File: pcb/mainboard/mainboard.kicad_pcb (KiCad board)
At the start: 10 copper layers, 165 x 121 mm, 629 parts, among them J1 CONN_PCIE_PWR_8PIN, J10 FAN_01, J11 XILINX_JTAG, J12 JUMPER_0402_SPDT, J13 JUMPER_0402_SPDT, J14 RJ45, J15 PMOD_HOST, J16 SMPM, J17 SMPM, J18 SMPM, J19 SMPM, J2 CONN_IBC_MGMT, J20 SMPM, J21 SMPM, J22 SMPM, J23 SMPM, J24 SMPM, J25 SMPM, J26 SMPM, J27 0826-1G1T-23-F, J28 SMPM, J29 SMPM, J3 CONN_01X03, J30 SMPM, J31 SMPM, J32 SMPM, J33 SMPM, J34 SMPM, J35 SMPM, J36 SMPM, J37 SMPM, J38 SMPM, J39 SMPM, J4 CONN_01X05, J40 SMPM, J41 SMPM, J42 SMPM, J43 SMPM, J44 SMPM, J45 SMPM, J46 SMPM, J47 SMPM, J48 CONN_01X10, J5 XILINX_JTAG, J6 CONN_SFP_HOST, J7 SFP_CAGE, J8 FAN_01, J9 CONN_01X03, K1 RELAY_TE_HF3_96, K2 RELAY_TE_HF3_96, K3 RELAY_TE_HF3_96, K4 RELAY_TE_HF3_96, M1 960-23-23-F-AB-0, SW1 SWITCH, SW2 SWITCH, U1 STM32L031C6U6, U10 MAX40026, U11 MAX40026, U12 MAX40026, U13 MAX40026, U14 MAX40026, U15 MAX40026, U16 MAX40026, U17 MAX40026, U18 MAX40026, U19 MAX40026, U2 MYMGK1R812ERSR, U20 MAX40026, U21 DAC60508, U22 DAC60508, U23 STM32H735-UFBGA176-25, U24 AT24MAC402, U25 ADM3101E_QFN, U26 LMR70503, U27 SIT9121AI-2BF-XXS200.000000G, U28 SIT9121AI-2BF-XXS156.250000G, U29 HMC675LP3E, U3 MYMGK00504ERSR, U30 SIT9121AI-2BF-XXS200.000000G, U31 ECS-1612MV-250-CN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

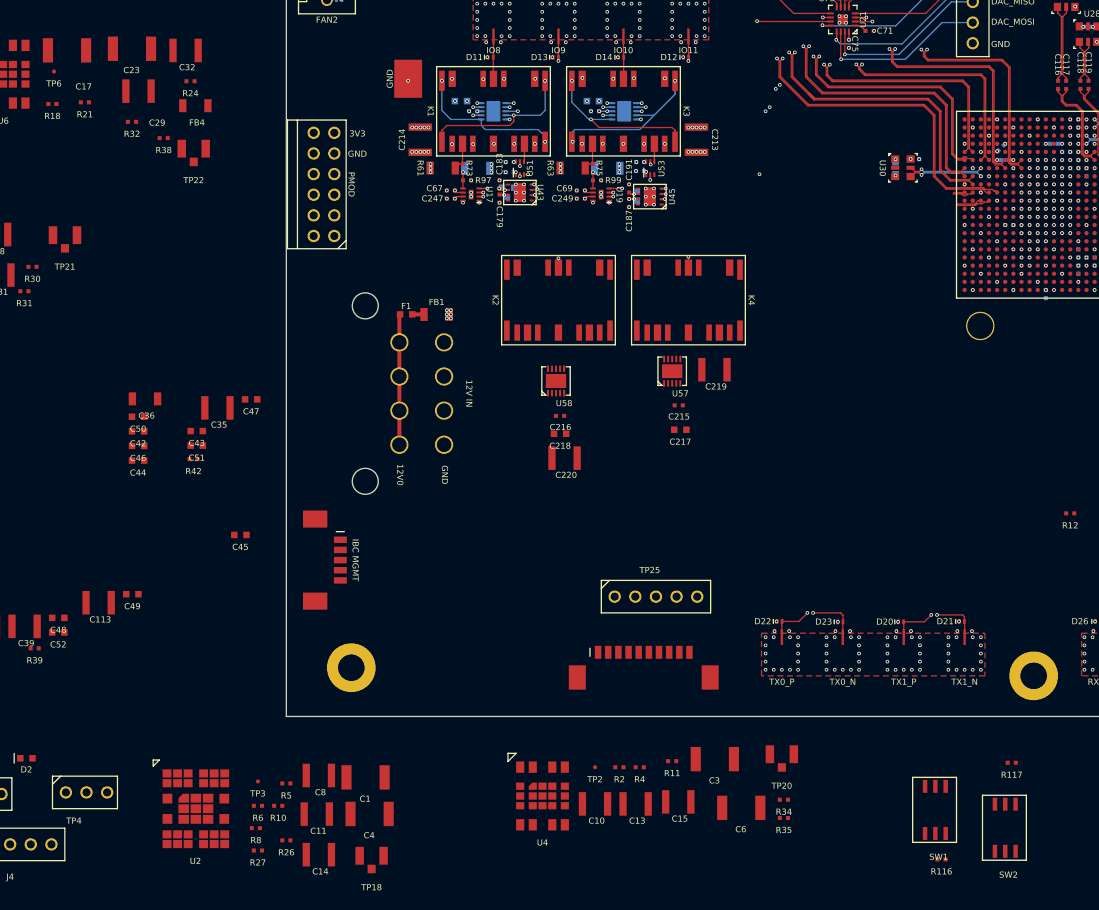
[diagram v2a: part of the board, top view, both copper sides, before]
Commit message: Placed remainder of relays and drivers
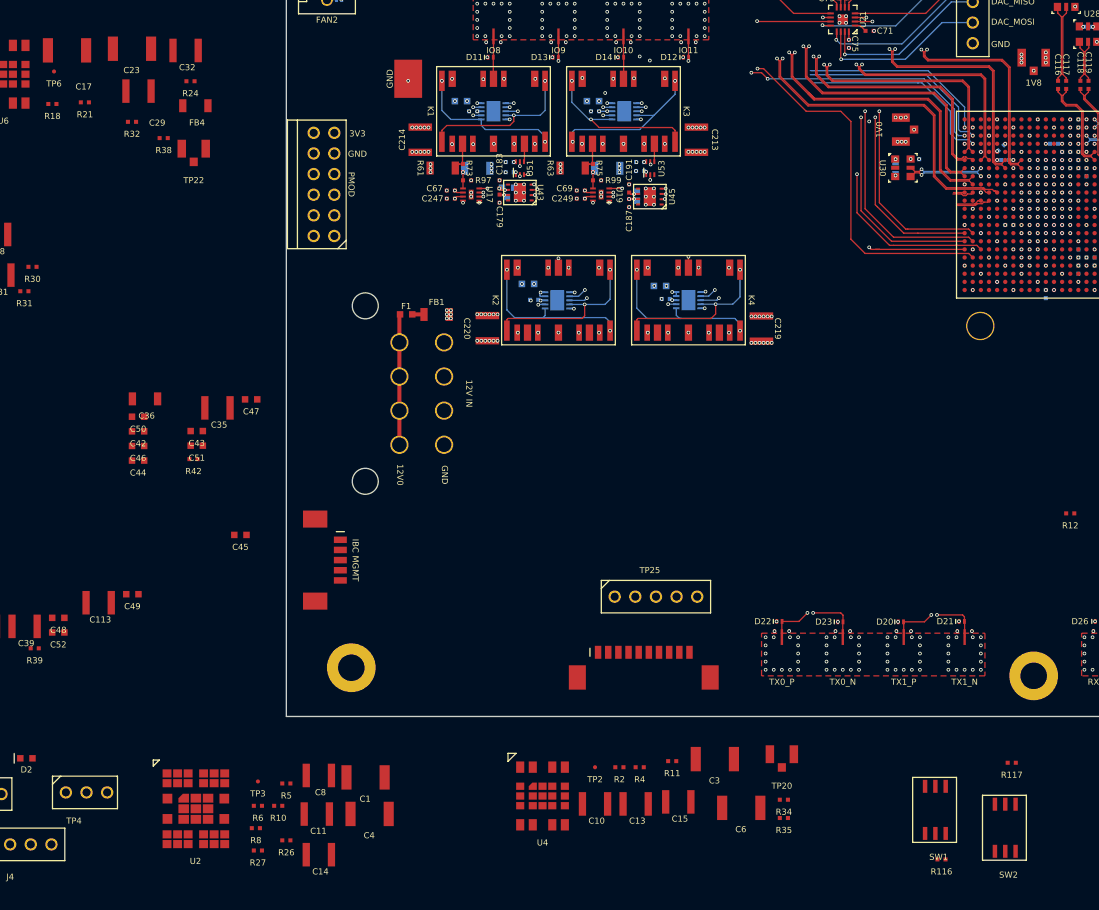
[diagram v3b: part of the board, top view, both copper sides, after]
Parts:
- C215, C216, C217, C218, U57, U58: moved to B.Cu
- moved TP21 121.2 mm to (207.0, 60.0)
- moved TP18 110.8 mm to (190.8, 68.8), turned to 90 degrees
- moved C218 18.9 mm to (144.8, 87.8), turned to 180 degrees
- moved C220 18.6 mm to (139.8, 93.2), turned to -90 degrees
- moved C217 17.9 mm to (161.0, 88.0), turned to 180 degrees
- moved C216 14.7 mm to (145.5, 89.7), turned to 180 degrees
- moved C215 13.2 mm to (161.7, 89.6), turned to 180 degrees
- moved U58 9.93 mm to (148.3, 89.8), turned to -90 degrees
- moved U57 8.98 mm to (164.5, 89.8), turned to -90 degrees
- moved C219 7.69 mm to (173.5, 93.2), turned to -90 degrees
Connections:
- U8 pad AA15: unconnected-(U8-PadAA15) -> /Connectors/OE8B
- U8 pad AA16: unconnected-(U8-PadAA16) -> /Connectors/OE10B
- U8 pad AA18: unconnected-(U8-PadAA18) -> /Output/OUT7_3V3
- U8 pad AA20: /Connectors/OE10B -> unconnected-(U8-PadAA20)
- U8 pad AB15: unconnected-(U8-PadAB15) -> /Connectors/OE8A
- U8 pad AB16: unconnected-(U8-PadAB16) -> /Connectors/OE10A
- U8 pad AB17: unconnected-(U8-PadAB17) -> /Output/OUT6_3V3
- U8 pad T18: /Output/OUT8_3V3 -> unconnected-(U8-PadT18)
- U8 pad T20: /Connectors/OE10A -> unconnected-(U8-PadT20)
- U8 pad U17: /Connectors/OE8A -> unconnected-(U8-PadU17)
- U8 pad U22: /Output/OUT6_3V3 -> unconnected-(U8-PadU22)
- U8 pad V22: /Output/OUT7_3V3 -> unconnected-(U8-PadV22)
- U8 pad Y17: unconnected-(U8-PadY17) -> /Output/OUT8_3V3
- U8 pad Y21: /Connectors/OE8B -> unconnected-(U8-PadY21)
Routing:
- net /GND: track 1975.1 -> 2124.7 mm, vias 1175 -> 1225
- net /Output/OUT6_3V3: track 14.1 -> 82.5 mm, vias 1 -> 4
- net /Output/OUT7_3V3: track 13.7 -> 72.9 mm, vias 1 -> 3
- net /Connectors/OUT3: track 32.6 -> 83.1 mm, vias 1 -> 5
- net /12V0: track 170.1 -> 216.8 mm, vias 34 -> 48
- net /3V3: track 753.1 -> 791.9 mm, vias 141 -> 147
- net /Output/OUT8_3V3: track 34.9 -> 63.0 mm
- net /Connectors/OUT0: track 29.9 -> 54.6 mm, vias 1 -> 2
- net /Connectors/OE10B: track 30.7 -> 55.3 mm
- net /Connectors/OE10A: track 29.4 -> 53.8 mm
- net /Connectors/OUT2: track 32.6 -> 56.9 mm, vias 1 -> 2
- net /Connectors/OUT1: track 32.6 -> 56.0 mm, vias 1 -> 2
- net /Connectors/OE8B: track 52.4 -> 74.5 mm
- net /Connectors/CH9_COIL_N: track 0.00 -> 21.4 mm, vias 0 -> 2
- net /Connectors/OE8A: track 51.6 -> 72.8 mm
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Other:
- board text added: "1V0"
- board text added: "1V8"

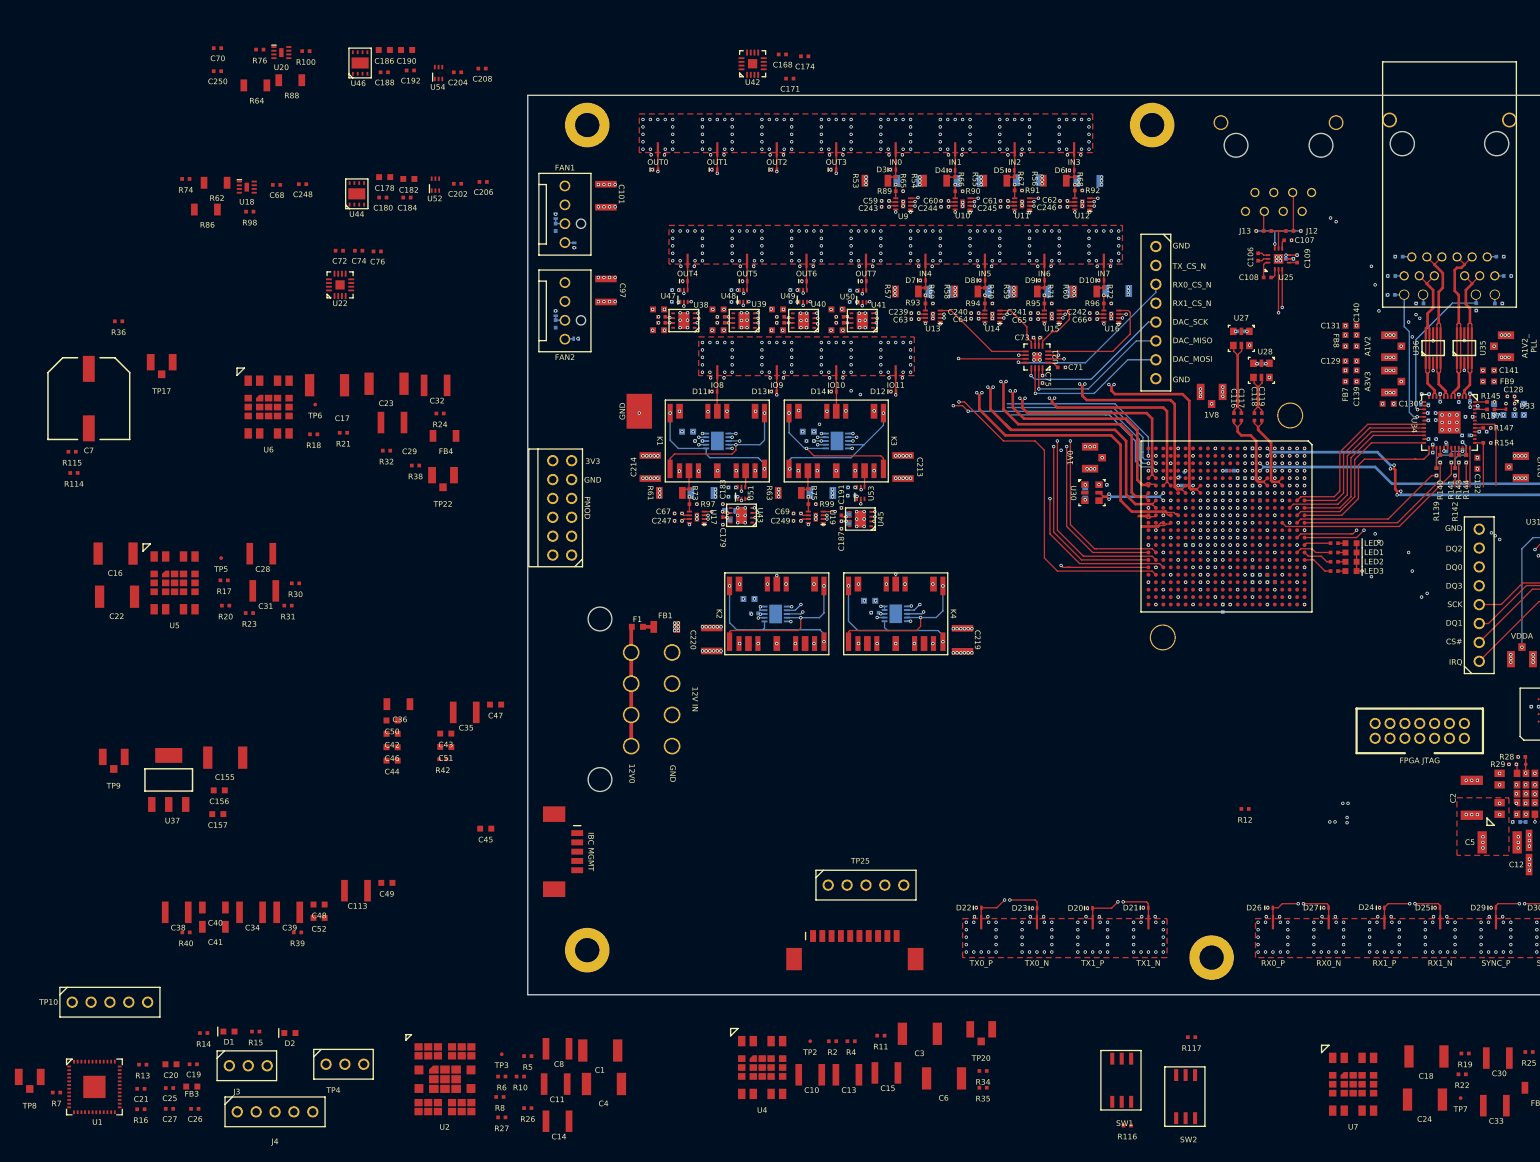
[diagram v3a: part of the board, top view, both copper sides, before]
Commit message: Tweaks to debug connectors, hooked up TX DAC
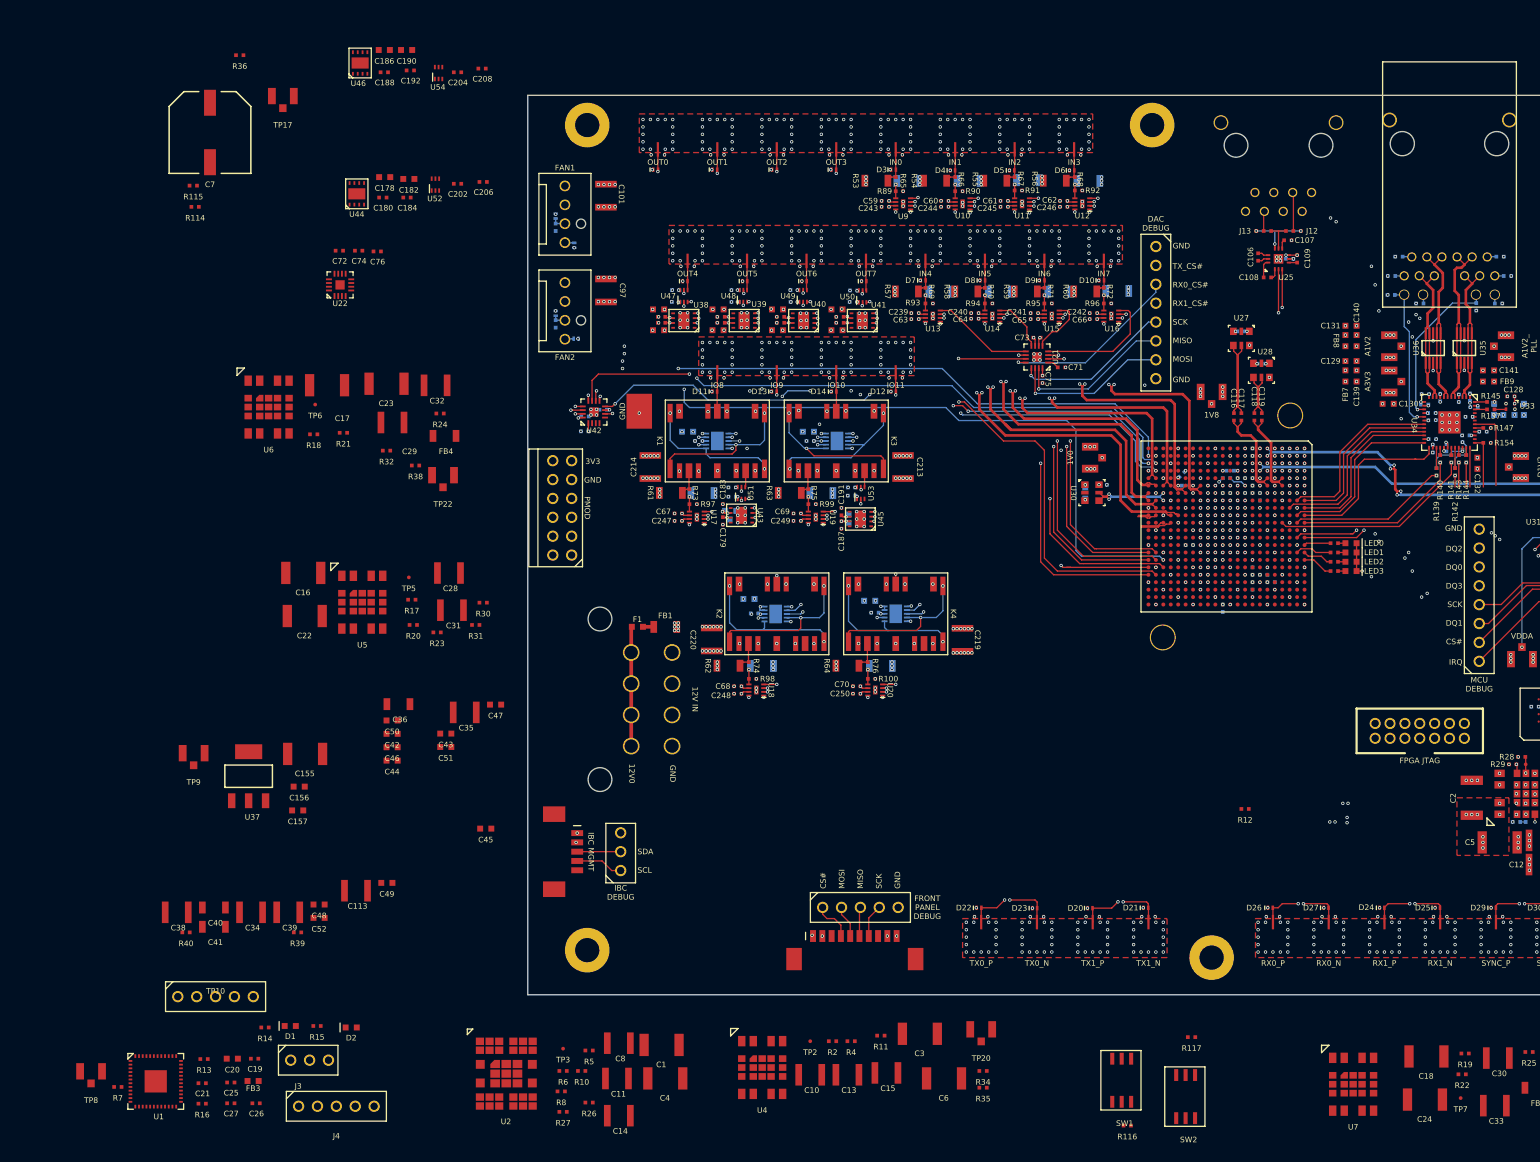
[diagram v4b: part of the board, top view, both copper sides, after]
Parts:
- C168, C171, C174, R42, R86, R88: moved to B.Cu
- moved C70 121.5 mm to (159.2, 99.5), turned to 180 degrees
- moved C250 120.0 mm to (159.2, 100.5), turned to 180 degrees
- moved U20 117.2 mm to (161.8, 100.0), turned to 180 degrees
- moved R76 116.5 mm to (160.8, 96.8), turned to -90 degrees
- moved R100 113.7 mm to (161.2, 98.5)
- moved R42 112.0 mm to (209.0, 71.5), turned to 180 degrees
- moved R88 111.9 mm to (162.5, 96.8), turned to 180 degrees
- moved R64 111.6 mm to (158.0, 96.8), turned to 180 degrees
- moved R74 100.1 mm to (144.8, 96.8), turned to -90 degrees
- moved R86 96.8 mm to (146.5, 96.8), turned to 180 degrees
- moved U18 96.3 mm to (145.8, 100.0), turned to 180 degrees
- moved R62 94.8 mm to (142.0, 96.8), turned to 180 degrees
- moved R98 92.3 mm to (145.2, 98.5)
- moved C68 91.6 mm to (143.2, 99.5), turned to 180 degrees
- moved C248 90.2 mm to (143.2, 100.5), turned to 180 degrees
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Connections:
- TP4 pad 1: /Power Supply/SUPER_I2C_SDA -> /Power Supply/SUPER_I2C_SCL
- TP4 pad 2: /Power Supply/SUPER_I2C_SCL -> /Power Supply/SUPER_I2C_SDA
- U42 pad 10: /Output/VREF_OUT6 -> /Output/VREF_OUT5
- U42 pad 11: /Output/VREF_OUT7 -> /Output/VREF_OUT4
- U42 pad 8: /Output/VREF_OUT4 -> /Output/VREF_OUT7
- U42 pad 9: /Output/VREF_OUT5 -> /Output/VREF_OUT6
- U8 pad AA3: /Connectors/OUT0 -> /Connectors/OUT1
- U8 pad AB18: unconnected-(U8-PadAB18) -> /Output/OUT5_3V3
- U8 pad AB2: /Connectors/OUT1 -> /Connectors/OUT0
- U8 pad T21: /Output/OUT4_3V3 -> unconnected-(U8-PadT21)
- U8 pad U21: /Output/OUT5_3V3 -> unconnected-(U8-PadU21)
- U8 pad Y16: unconnected-(U8-PadY16) -> /Output/OUT4_3V3
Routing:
- net /3V3_SB: track 45.7 -> 203.1 mm, vias 2 -> 4
- net /DAC_MOSI: track 39.2 -> 175.8 mm, vias 2 -> 6
- net /GND: track 2124.7 -> 2225.6 mm, vias 1225 -> 1260
- net /TX_DAC_CS_N: track 99.0 -> 196.3 mm, vias 3 -> 6
- net /Output/OUT4_3V3: track 12.3 -> 97.2 mm, vias 1 -> 3
- net /DAC_MISO: track 110.7 -> 189.0 mm, vias 4 -> 6
- net /3V3: track 791.9 -> 868.5 mm, vias 147 -> 153
- net /Output/OUT5_3V3: track 14.0 -> 90.4 mm, vias 1 -> 3
- net /DAC_SCK: track 110.7 -> 177.5 mm, vias 4 -> 6
- net /Connectors/OUT0: track 54.6 -> 101.3 mm, vias 2 -> 3
- net /Connectors/OUT1: track 56.0 -> 100.1 mm, vias 2 -> 3
- net /Output/VREF_OUT7: track 11.0 -> 49.2 mm, vias 1 -> 3
- net /Connectors/OUT2: track 56.9 -> 92.9 mm, vias 2 -> 4
- net /FPGA Support/GTX_1V8: track 9.71 -> 42.4 mm
- net /Output/VREF_OUT6: track 15.1 -> 40.4 mm, vias 1 -> 4
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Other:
- board text added: "DAC DEBUG"
- board text added: "FRONT PANEL DEBUG"
- board text added: "IBC DEBUG"
- board text added: "MCU DEBUG"
- board text added: "MISO"
- board text added: "MOSI"
- board text added: "RX0_CS#"
- board text added: "RX1_CS#"
- board text added: "SCL"
- board text added: "SDA"
- board text added: "TX_CS#"
- board text removed: "DAC_MISO"
- board text removed: "DAC_MOSI"
- board text removed: "DAC_SCK"
- board text removed: "RX0_CS_N"
- board text removed: "RX1_CS_N"
- board text removed: "TX_CS_N"

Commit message: Hooked up soft power/reset buttons
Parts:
- R116, R117, R36: moved to B.Cu
- moved C17 215.2 mm to (295.9, 115.0)
- moved C23 215.2 mm to (303.9, 114.8)
- moved R18 215.2 mm to (294.1, 121.5)
- moved R21 215.2 mm to (298.1, 121.3)
- moved U6 215.2 mm to (288.0, 117.9)
- moved TP6 215.2 mm to (294.2, 117.5)
- moved R24 208.8 mm to (300.6, 130.8)
- moved C32 208.8 mm to (300.0, 127.0)
- moved C29 199.4 mm to (286.0, 127.0)
- moved R38 198.7 mm to (288.6, 132.3)
- moved TP22 198.7 mm to (292.2, 133.8)
- moved FB4 198.7 mm to (292.4, 128.3)
- moved R32 198.7 mm to (284.6, 130.3)
- moved C186 122.9 mm to (169.8, 112.0)
- moved C188 122.9 mm to (169.8, 115.0)
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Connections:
- SW1 pad 2: /3V3 -> /3V3_SB
- SW2 pad 2: /3V3 -> /3V3_SB
- U8 pad AA10: /Inputs/TRIGIN_9_P -> unconnected-(U8-PadAA10)
- U8 pad AA20: unconnected-(U8-PadAA20) -> /Connectors/OE11A
- U8 pad AA21: unconnected-(U8-PadAA21) -> /Output/OUT9_3V3
- U8 pad AB10: /Inputs/TRIGIN_9_N -> unconnected-(U8-PadAB10)
- U8 pad AB20: unconnected-(U8-PadAB20) -> /Output/OUT10_3V3
- U8 pad AB22: unconnected-(U8-PadAB22) -> /Connectors/OE9A
- U8 pad T10: /Inputs/TRIGIN_11_N -> /Inputs/TRIGIN_8_N
- U8 pad T11: /Inputs/TRIGIN_11_P -> /Inputs/TRIGIN_8_P
- U8 pad T15: unconnected-(U8-PadT15) -> /Output/OUT4_3V3
- U8 pad T8: unconnected-(U8-PadT8) -> /Inputs/TRIGIN_10_N
- U8 pad T9: unconnected-(U8-PadT9) -> /Inputs/TRIGIN_10_P
- U8 pad U18: /Output/OUT9_3V3 -> unconnected-(U8-PadU18)
- U8 pad U20: /Connectors/OE11A -> unconnected-(U8-PadU20)
- U8 pad U8: /Inputs/TRIGIN_8_P -> /Inputs/TRIGIN_11_P
- U8 pad V18: /Connectors/OE9A -> unconnected-(U8-PadV18)
- U8 pad V8: /Inputs/TRIGIN_8_N -> /Inputs/TRIGIN_11_N
- U8 pad W11: /Inputs/TRIGIN_10_P -> /Inputs/TRIGIN_9_P
- U8 pad W21: /Output/OUT10_3V3 -> unconnected-(U8-PadW21)
- U8 pad Y11: /Inputs/TRIGIN_10_N -> /Inputs/TRIGIN_9_N
- U8 pad Y16: /Output/OUT4_3V3 -> unconnected-(U8-PadY16)
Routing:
- net /Inputs/TRIGIN_8_P: track 5.13 -> 72.5 mm, vias 1 -> 2
- net /Inputs/TRIGIN_8_N: track 5.13 -> 72.2 mm, vias 1 -> 2
- net /FPGA_DONE: track 10.5 -> 76.8 mm, vias 2 -> 4
- net /FLASH_SCK: track 3.96 -> 65.8 mm
- net /FPGA Support/FPGA_JTAG_TDO: track 0.71 -> 59.4 mm, vias 1 -> 2
- net /FPGA Support/FPGA_JTAG_TDI: track 0.00 -> 56.2 mm, vias 1 -> 2
- net /Management/FLASH_DQ0: track 10.3 -> 64.9 mm
- net /FPGA Support/FPGA_JTAG_TMS: track 0.00 -> 52.6 mm, vias 1 -> 2
- net /FPGA Support/FPGA_JTAG_TCK: track 0.00 -> 52.4 mm, vias 1 -> 2
- net /Management/FLASH_CS_N: track 5.06 -> 55.3 mm, vias 1 -> 2
- net /Management/FLASH_DQ2: track 5.00 -> 53.3 mm, vias 1 -> 2
- net /Inputs/TRIGIN_10_N: track 8.75 -> 56.5 mm, vias 1 -> 2
- net /Management/FLASH_DQ1: track 8.16 -> 55.9 mm, vias 1 -> 2
- net /Inputs/TRIGIN_10_P: track 9.82 -> 56.8 mm, vias 1 -> 2
- net /Management/FLASH_DQ3: track 6.21 -> 52.8 mm, vias 1 -> 2
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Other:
- board text added: "PWR"
- board text added: "RST"
- board text removed: "12V input"
- board text removed: "INPUTS"
- board text removed: "Power switches"
